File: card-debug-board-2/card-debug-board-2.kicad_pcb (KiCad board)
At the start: 2 copper layers, 36 x 52 mm, 30 parts, among them J1 2-1734592-0, J2 Conn_01x05, J5 0676430910, J6 629105150521, SW1 PCM13SMTR, SW2 B3F-1000, SW3 CFS-0103TB, SW4 CFS-0103TB, U1 MIC5205-3.3YM5

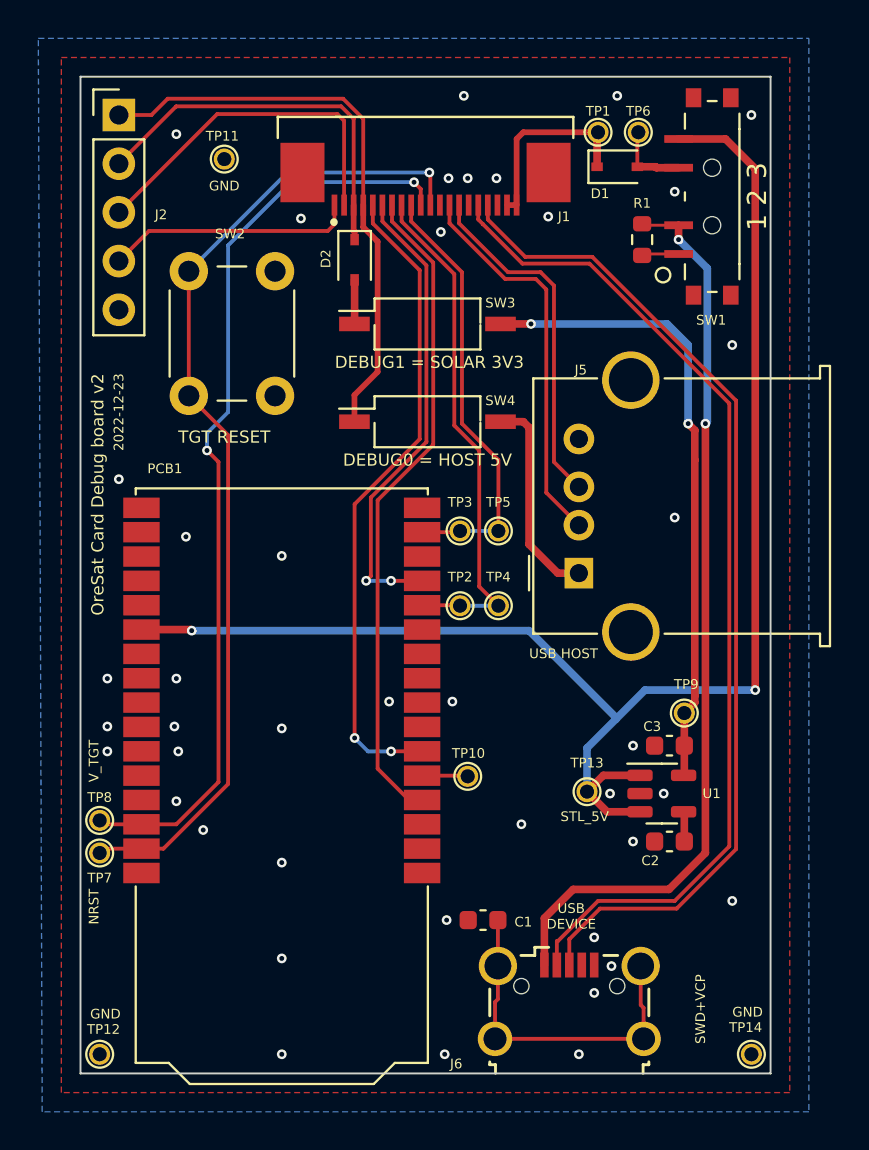
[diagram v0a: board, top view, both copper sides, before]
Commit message: Modified debug board, removed several peripherals
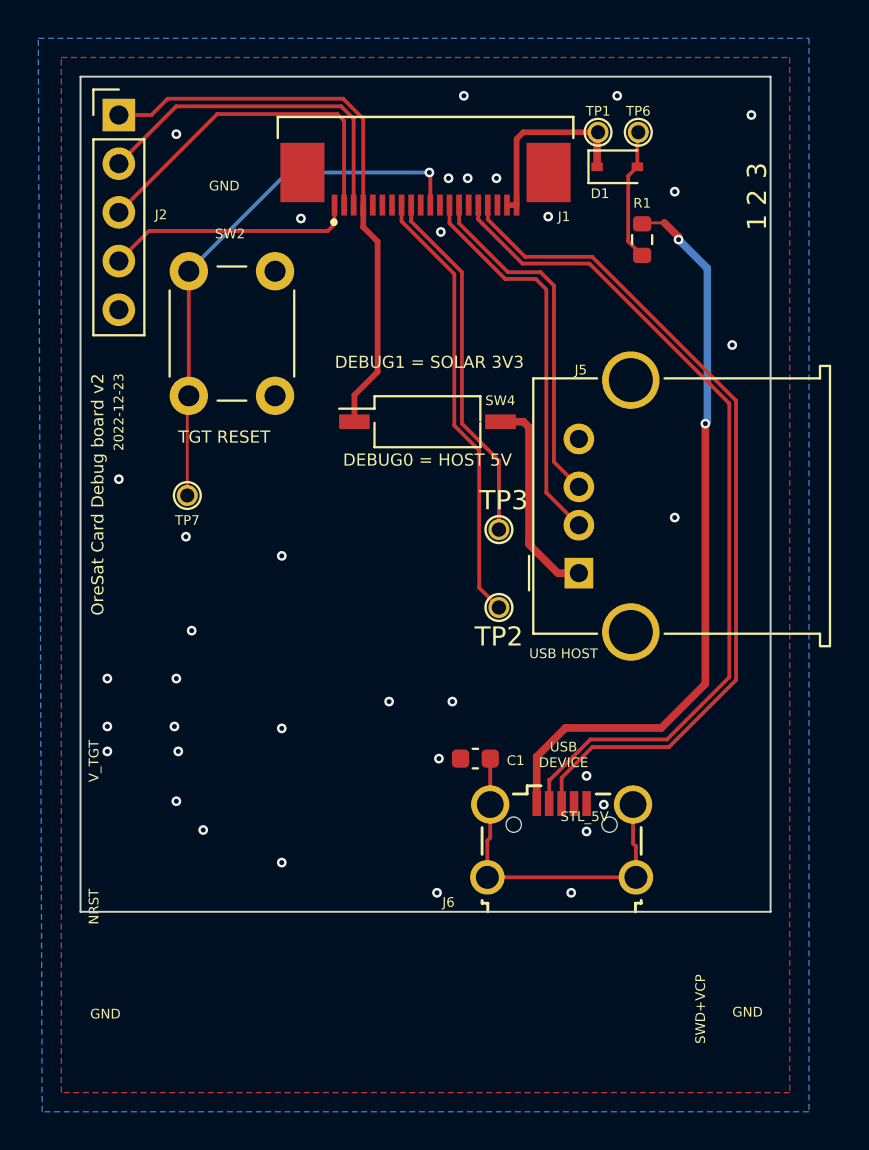
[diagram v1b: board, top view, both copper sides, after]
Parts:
- removed C2: 470p, Capacitor_SMD:C_0603_1608Metric
- removed C3: 2.2u, Capacitor_SMD:C_0603_1608Metric
- removed D2: ZLLS410TA, Diode_SMD:D_SOD-323
- removed PCB1: STLINK-V3MODS, oresat-pcbs:STLINK-V3MOS
- removed SW1: PCM13SMTR, oresat-misc:SW-CK-PCM13SMTR
- removed SW3: CFS-0103TB, Button_Switch_SMD:SW_DIP_SPSTx01_Slide_Copal_CHS-01B_W7.62mm_P1.27mm
- removed TP10, TP11, TP12, TP13, TP14, TP4, TP5, TP8, TP9: TestPoint-MinTH, oresat-misc:TestPoint-MinTH
- removed U1: MIC5205-3.3YM5, Package_TO_SOT_SMD:SOT-23-5
- TP2, TP3: footprint oresat-misc:TestPoint-MinTH -> oresat-misc:TestPoint-0.75mm-th
- moved TP7 19.2 mm to (131.6, 69.8)
- moved C1 8.43 mm to (146.6, 83.6)
- moved J6 8.43 mm to (151.1, 87.8)
- moved TP2 2.03 mm to (147.8, 75.7)
- moved TP3 2.03 mm to (147.8, 71.6)
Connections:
- J1 pad 11: Net-(J1-VTARGET) -> unconnected-(J1-VTARGET-Pad11)
- J1 pad 14: Net-(J1-SWDIO) -> unconnected-(J1-SWDIO-Pad14)
- J1 pad 15: Net-(J1-SWCLK) -> unconnected-(J1-SWCLK-Pad15)
- J1 pad 16: Net-(J1-SWO) -> unconnected-(J1-SWO-Pad16)
- R1 pad 2: Net-(R1-Pad2) -> Net-(D1-A)
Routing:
- net +5V: track 77.1 -> 0.00 mm, vias 2 -> 0
- net Net-(J1-VTARGET): track 48.4 -> 0.00 mm, vias 2 -> 0
- net Net-(J1-SWDIO): track 34.5 -> 0.00 mm
- net Net-(J1-SWO): track 34.0 -> 0.00 mm, vias 2 -> 0
- net +3.3V: track 33.1 -> 0.00 mm, vias 2 -> 0
- net Net-(J1-SWCLK): track 24.8 -> 0.00 mm, vias 2 -> 0
- net Net-(J1-NRST): track 52.2 -> 28.1 mm
- net Net-(J6-VBUS): track 47.6 -> 39.0 mm
- net Net-(J1-DEVICE-D-): track 53.2 -> 45.0 mm
- net Net-(J1-DEVICE-D+): track 53.0 -> 44.8 mm
- net Net-(J1-CARD-RX): track 22.9 -> 18.8 mm
- net Net-(J1-CARD-TX): track 27.0 -> 23.1 mm
- net Net-(D1-A): track 4.00 -> 7.05 mm
- net Net-(PCB1-GNDDETECT): track 2.39 -> 0.00 mm
- net Net-(D2-A): track 2.30 -> 0.00 mm
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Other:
- board size 36 x 52 mm -> 36 x 43.6 mm

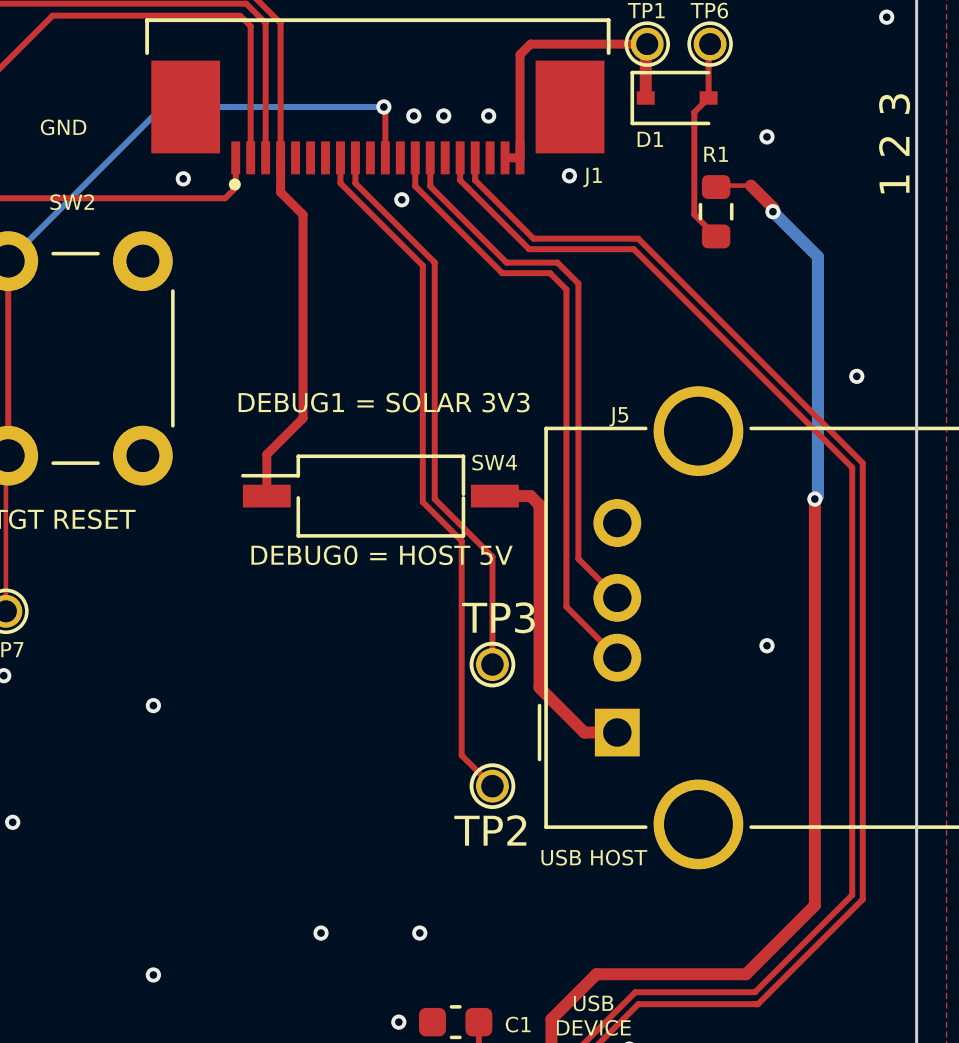
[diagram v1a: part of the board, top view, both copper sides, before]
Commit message: Added proper connector for UART and changed 10k ohm resistor on the VBUS line to 0 ohm
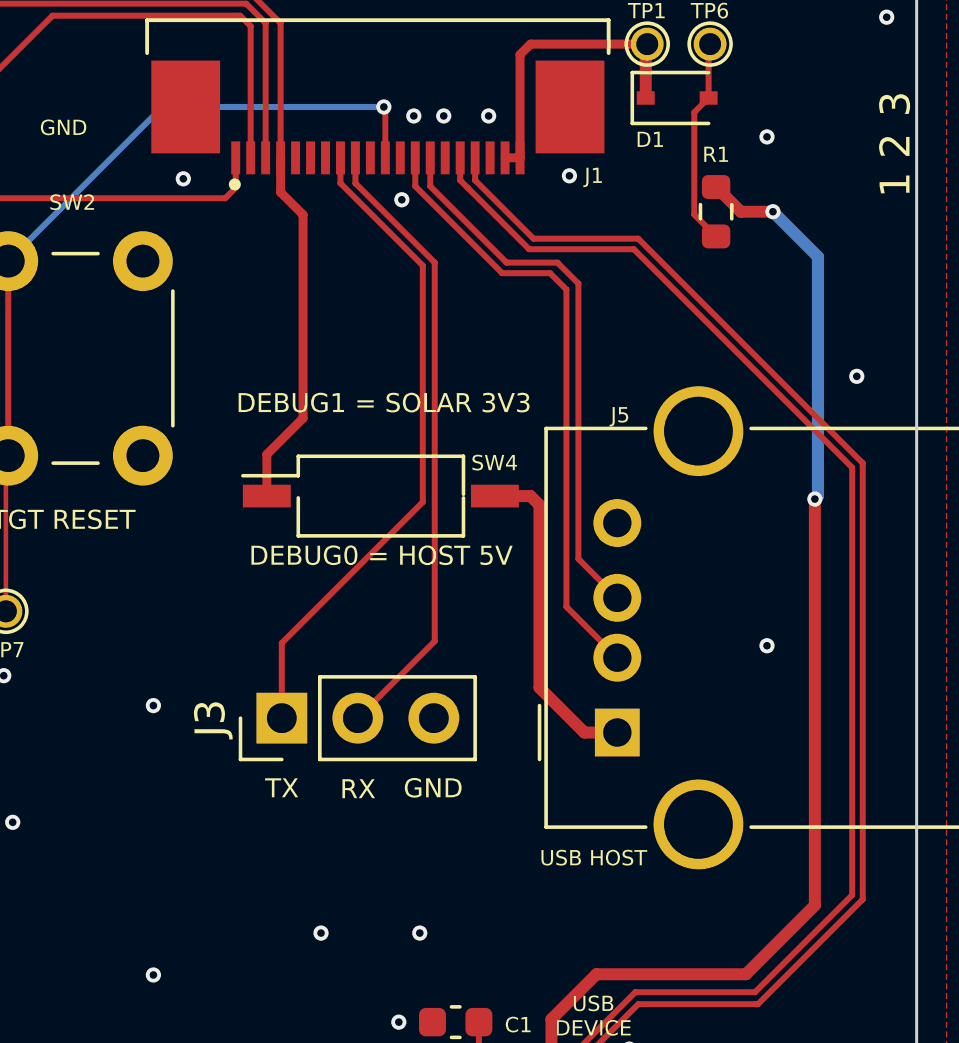
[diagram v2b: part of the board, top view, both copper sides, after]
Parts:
- removed TP2, TP3: TestPoint-MinTH, oresat-misc:TestPoint-0.75mm-th
- added J3: Conn_01x03, Connector_PinHeader_2.54mm:PinHeader_1x03_P2.54mm_Vertical, F.Cu at (140.8, 73.4)
- J1: value 2-1734592-0 -> 2-1734592-0
- R1: value 10k -> 0
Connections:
- J1 pad 12: Net-(J1-CARD-RX) -> UART0_RX
- J1 pad 13: Net-(J1-CARD-TX) -> UART0_TX
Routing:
- net Net-(J1-CARD-TX): track 23.1 -> 0.00 mm
- net UART0_TX: track 0.00 -> 21.8 mm
- net UART0_RX: track 0.00 -> 20.9 mm
- net Net-(J1-CARD-RX): track 18.8 -> 0.00 mm
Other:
- board text added: "RX"
- board text added: "TX"
